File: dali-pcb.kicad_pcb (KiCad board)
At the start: 2 copper layers, 180.5 x 113 mm, 60 parts, among them J1 12-22.5V DC, J10 5V DC, J11 5V DC, J12 5V DC, J13 5V DC, J14 5V DC, J15 GND, J2 DALI BUS, J20 LOLIN-S3 (L), J21 LOLIN-S3 (R), J22 ESP32-S3-DEVKITC-1 (L), J23 ESP32-S3-DEVKITC-1 (R), J24 LOLIN-S3-MINI (L), J25 LOLIN-S3-MINI (R), J26 LOLIN-S2-MINI (L), J27 LOLIN-S2-MINI (R), J3 DALI BUS, J30 FTDI-MCU, J31 UART-DALI, J4 DALI BUS, J40 A10-0, J41 A5-0, J42 A5-5, J43 A2-0, J44 A2-2, J45 A2-4, J46 A2-6, J47 A2-8, J50 D8-11, J51 D4-11, J52 D4-16, J53 D2-11, J54 D2-13, J55 D2-16, J56 D2-18, J60 D1-11, J61 D1-12, J62 D1-13, J63 D1-14, Q1 PZT2222A, Q2 MMBT2222A, U1 TCLT1000, U2 TCLT1000

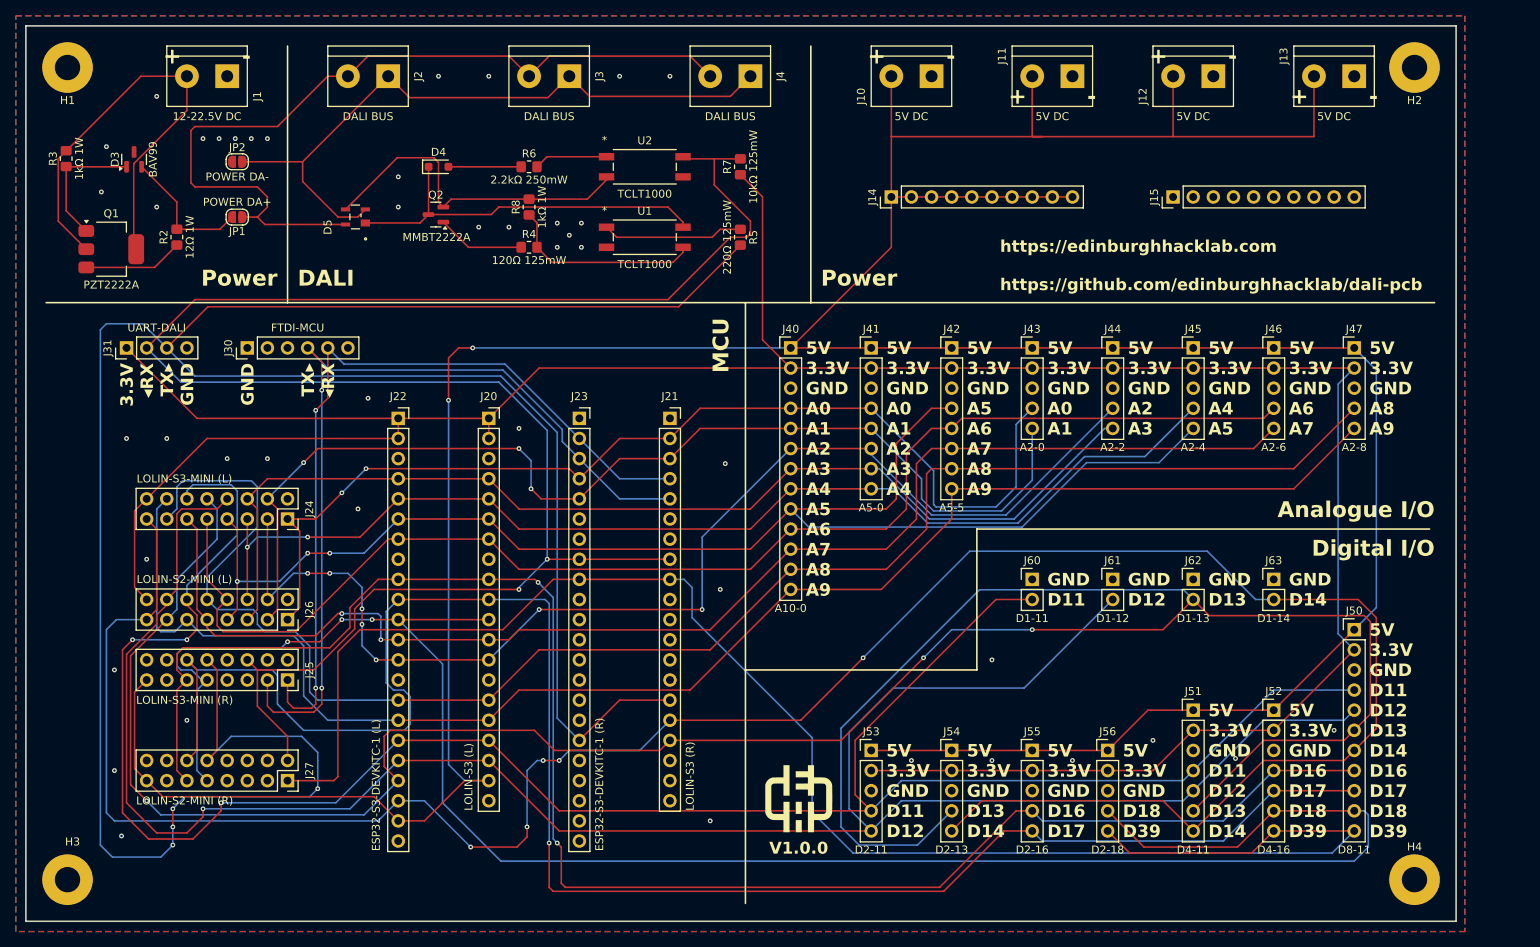
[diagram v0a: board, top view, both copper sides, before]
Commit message: Add solder jumpers to bypass the bridge rectifier
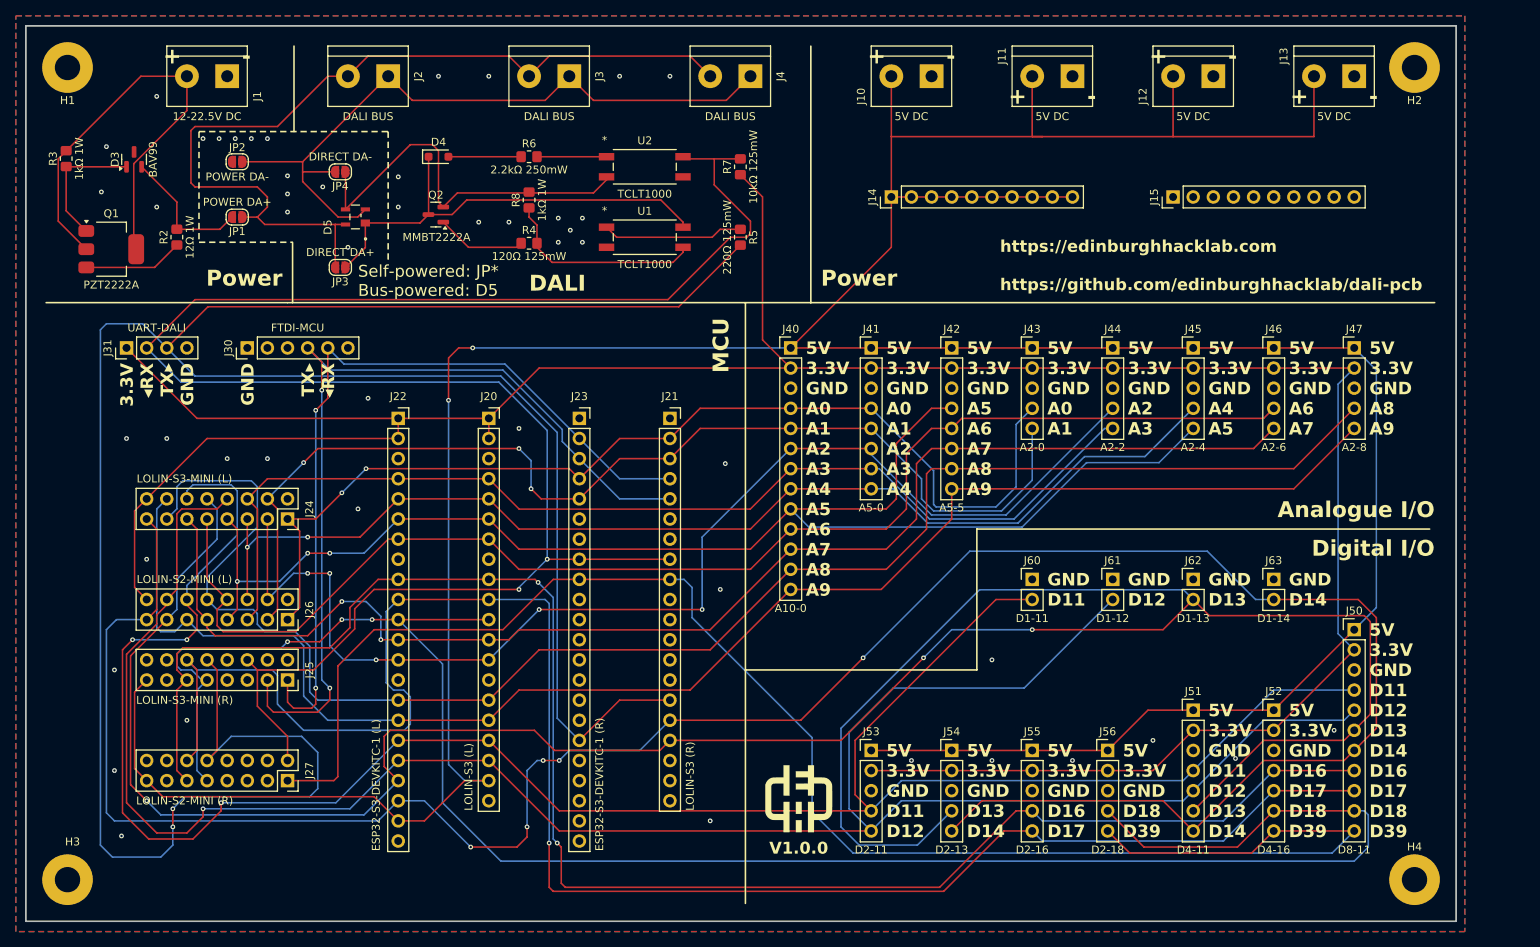
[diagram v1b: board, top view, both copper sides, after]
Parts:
- added JP3: DIRECT DA+, Jumper:SolderJumper-2_P1.3mm_Open_RoundedPad1.0x1.5mm, F.Cu at (54.9, 45.7)
- added JP4: DIRECT DA-, Jumper:SolderJumper-2_P1.3mm_Open_RoundedPad1.0x1.5mm, F.Cu at (54.9, 33.7)
- moved D4 1.27 mm to (67.3, 31.8)
- moved R6 1.27 mm to (78.7, 31.8)
- moved R8 0.89 mm to (78.7, 37.2)
- moved R4 0.51 mm to (78.7, 42.7)
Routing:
- net Net-(D4-K): track 48.4 -> 57.0 mm
- net Net-(D5--): track 43.0 -> 49.9 mm
- net /DALI/DA+: track 106.0 -> 111.5 mm
- net /DALI/DA-: track 85.6 -> 90.4 mm
- net /IO/IO_A7: track 169.2 -> 170.5 mm
- net /IO/IO_D18: track 248.5 -> 247.3 mm
- net /IO/FTDI_MCU_TXD: track 111.1 -> 112.2 mm
- net /IO/IO_D39: track 211.0 -> 210.0 mm
- net /IO/IO_A2: track 152.9 -> 154.0 mm, vias 7 -> 5
- net /IO/IO_D11: track 271.7 -> 271.0 mm
- net /IO/IO_D12: track 271.0 -> 270.3 mm
- net Net-(R6-Pad2): track 9.31 -> 8.78 mm
- net GND: vias 44 -> 49
- net /DALI/DALI_TX: vias 4 -> 2
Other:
- board text added: "Self-powered: JP* Bus-powered: D5"

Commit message: Add more silkscreen to explain where things are
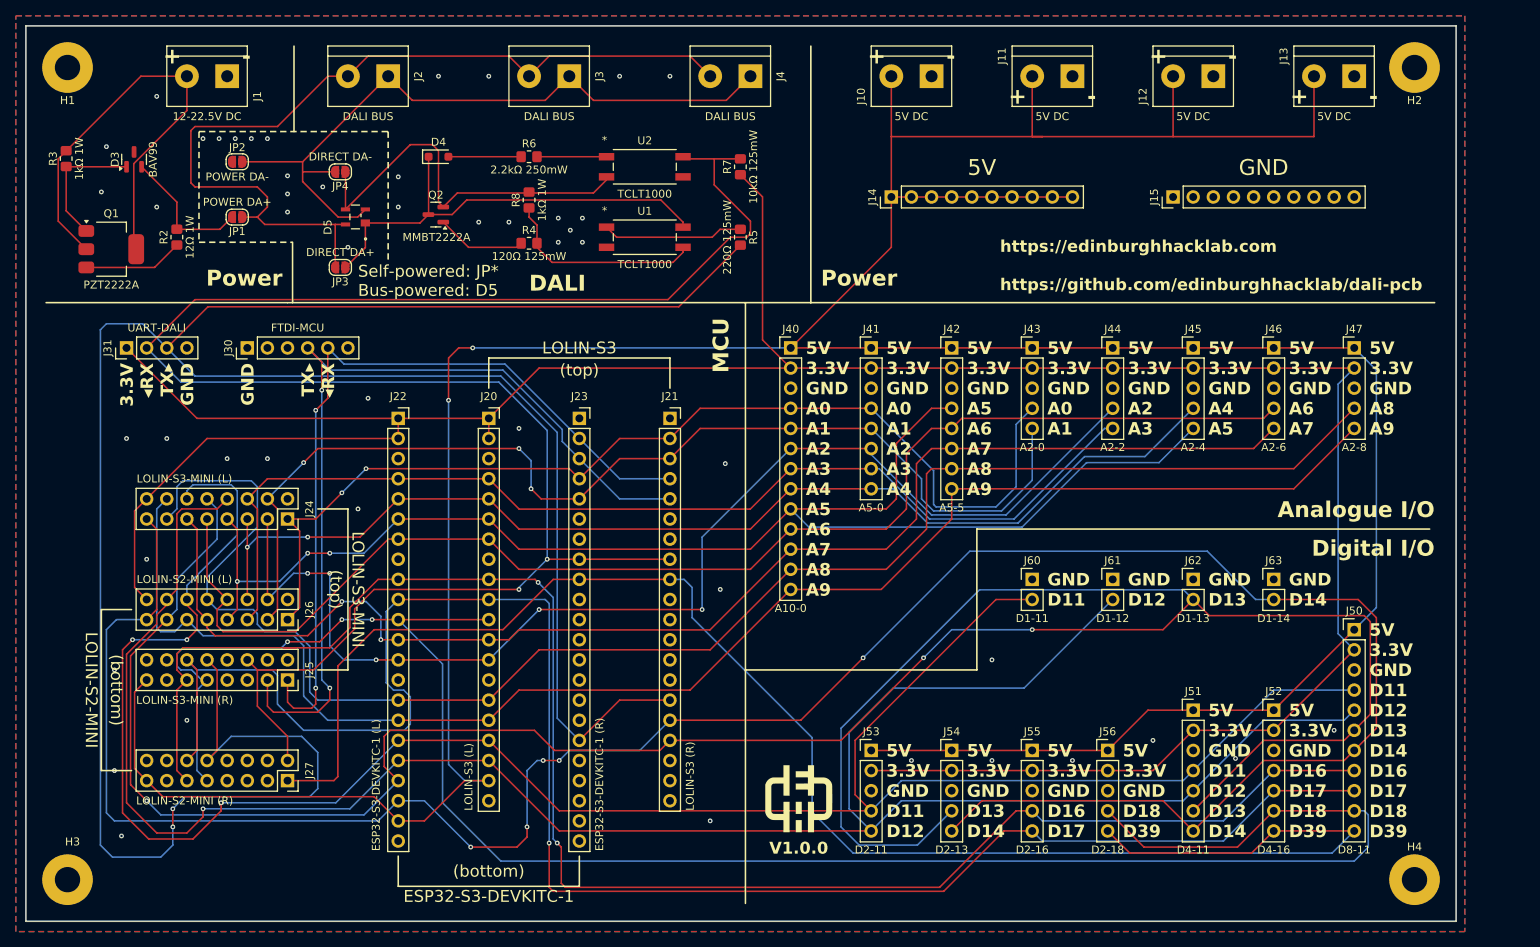
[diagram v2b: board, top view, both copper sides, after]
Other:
- board text added: "(bottom)"
- board text added: "(top)"
- board text added: "5V"
- board text added: "ESP32-S3-DEVKITC-1"
- board text added: "GND"
- board text added: "LOLIN-S2-MINI"
- board text added: "LOLIN-S3"
- board text added: "LOLIN-S3-MINI"
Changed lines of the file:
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@@
+	)
+	(gr_line
+		(start 73.66 57.15)
+		(end 96.52 57.15)
+		(stroke
+			(width 0.2)
+			(type solid)
+		)
+		(layer "F.SilkS")
 	)
 	(gr_line
@@
 	)
 	(gr_line
+		(start 85.09 123.825)
+		(end 62.23 123.825)
+		(stroke
+			(width 0.2)
+			(type solid)
+		)
+		(layer "F.SilkS")
+	)
+	(gr_line
 		(start 48.895 42.545)
 		(end 48.895 50.165)
@@
 	)
 	(gr_line
+		(start 24.765 109.22)
+		(end 28.575 109.22)
+		(stroke
+			(width 0.2)
+			(type solid)
+		)
+		(layer "F.SilkS")
+	)
+	(gr_line
 		(start 114.3 17.78)
 		(end 114.3 50.165)
@@
 	)
 	(gr_line
+		(start 96.52 57.15)
+		(end 96.52 60.96)
+		(stroke
+			(width 0.2)
+			(type solid)
+		)
+		(layer "F.SilkS")
+	)
+	(gr_line
 		(start 135.255 78.74)
 		(end 192.405 78.74)
@@
 	)
 	(gr_line
+		(start 55.88 76.2)
+		(end 52.07 76.2)
+		(stroke
+			(width 0.2)
+			(type solid)
+		)
+		(layer "F.SilkS")
+	)
+	(gr_line
+		(start 55.88 76.2)
+		(end 55.88 96.52)
+		(stroke
+			(width 0.2)
+			(type solid)
+		)
+		(layer "F.SilkS")
+	)
+	(gr_line
 		(start 37.084 28.575)
 		(end 37.084 42.545)
@@
 	)
 	(gr_line
+		(start 24.765 88.9)
+		(end 28.575 88.9)
+		(stroke
+			(width 0.2)
+			(type solid)
+		)
+		(layer "F.SilkS")
+	)
+	(gr_line
+		(start 73.66 57.15)
+		(end 73.66 60.96)
+		(stroke
+			(width 0.2)
+			(type solid)
+		)
+		(layer "F.SilkS")
+	)
+	(gr_line
+		(start 55.88 96.52)
+		(end 52.07 96.52)
+		(stroke
+			(width 0.2)
+			(type solid)
+		)
+		(layer "F.SilkS")
+	)
+	(gr_line
+		(start 85.09 123.825)
+		(end 85.09 120.015)
+		(stroke
+			(width 0.2)
+			(type solid)
+		)
+		(layer "F.SilkS")
+	)
+	(gr_line
 		(start 106.045 50.165)
 		(end 106.045 125.984)
@@
 		(start 106.045 96.52)
 		(end 135.255 96.52)
+		(stroke
+			(width 0.2)
+			(type solid)
+		)
+		(layer "F.SilkS")
+	)
+	(gr_line
+		(start 62.23 123.825)
+		(end 62.23 120.015)
+		(stroke
+			(width 0.2)
+			(type solid)
+		)
+		(layer "F.SilkS")
+	)
+	(gr_line
+		(start 24.765 109.22)
+		(end 24.765 88.9)
 		(stroke
 			(width 0.2)
@@
 		)
 	)
+	(gr_text "5V"
+		(at 135.89 34.29 0)
+		(layer "F.SilkS")
+		(effects
+			(font
+				(size 2 2)
+				(thickness 0.25)
+			)
+			(justify bottom)
+		)
+	)
+	(gr_text "GND"
+		(at 171.45 34.29 0)
+		(layer "F.SilkS")
+		(effects
+			(font
+				(size 2 2)
+				(thickness 0.25)
+			)
+			(justify bottom)
+		)
+	)
 	(gr_text "5V\n3.3V\nGND\nA6\nA7"
 		(at 174.625 54.991 0)
@@
 		)
 	)
+	(gr_text "LOLIN-S3-MINI"
+		(at 57.15 86.36 270)
+		(layer "F.SilkS")
+		(effects
+			(font
+				(size 1.5 1.5)
+				(thickness 0.1875)
+			)
+		)
+	)
 	(gr_text "+        -"
 		(at 144.78 24.13 0)
@@
 		)
 	)
+	(gr_text "LOLIN-S2-MINI"
+		(at 23.495 99.06 270)
+		(layer "F.SilkS")
+		(effects
+			(font
+				(size 1.5 1.5)
+				(thickness 0.1875)
+			)
+		)
+	)
+	(gr_text "LOLIN-S3"
+		(at 85.09 55.88 0)
+		(layer "F.SilkS")
+		(effects
+			(font
+				(size 1.5 1.5)
+				(thickness 0.1875)
+			)
+		)
+	)
 	(gr_text "+        -"
 		(at 162.56 19.05 0)
@@
 			)
 			(justify left top)
+		)
+	)
+	(gr_text "(top)"
+		(at 85.09 58.674 0)
+		(layer "F.SilkS")
+		(effects
+			(font
+				(size 1.5 1.5)
+				(thickness 0.1875)
+			)
 		)
 	)
@@
 		)
 	)
+	(gr_text "ESP32-S3-DEVKITC-1"
+		(at 73.66 125.095 0)
+		(layer "F.SilkS")
+		(effects
+			(font
+				(size 1.5 1.5)
+				(thickness 0.1875)
+			)
+		)
+	)
 	(gr_text "+        -"
 		(at 180.34 24.13 0)
@@
 		)
 	)
+	(gr_text "(bottom)"
+		(at 73.66 121.92 0)
+		(layer "F.SilkS")
+		(effects
+			(font
+				(size 1.5 1.5)
+				(thickness 0.1875)
+			)
+		)
+	)
 	(gr_text "5V\n3.3V\nGND\nA0\nA1"
 		(at 144.145 54.991 0)
@@
 		)
 	)
+	(gr_text "(top)"
+		(at 54.356 86.36 270)
+		(layer "F.SilkS")
+		(effects
+			(font
+				(size 1.5 1.5)
+				(thickness 0.1875)
+			)
+		)
+	)
 	(gr_text "Analogue I/O"
 		(at 193.04 77.47 0)
@@
 		)
 	)
+	(gr_text "(bottom)"
+		(at 26.67 99.06 270)
+		(layer "F.SilkS")
+		(effects
+			(font
+				(size 1.5 1.5)
+				(thickness 0.1875)
+			)
+		)
+	)
